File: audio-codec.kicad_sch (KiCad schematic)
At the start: 0 parts

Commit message: wip: not much to report yet
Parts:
- added U4: ~, symbol Library:TAC5112
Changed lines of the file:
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@@
 	(generator_version "8.0")
 	(paper "USLetter")
+	(symbol
+		(lib_id "Library:TAC5112")
+		(at 95.25 62.23 0)
+		(unit 1)
+		(exclude_from_sim no)
+		(in_bom yes)
+		(on_board yes)
+		(dnp no)
+		(fields_autoplaced yes)
+		(property "Reference" "U4"
+			(at 128.905 60.96 0)
+			(effects
+				(font
+					(size 1.27 1.27)
+				)
+			)
+		)
+		(property "Value" "~"
+			(at 128.905 63.5 0)
+			(effects
+				(font
+					(size 1.27 1.27)
+				)
+			)
+		)
+		(property "Footprint" ""
+			(at 95.25 62.23 0)
+			(effects
+				(font
+					(size 1.27 1.27)
+				)
+				(hide yes)
+			)
+		)
+		(property "Datasheet" ""
+			(at 95.25 62.23 0)
+			(effects
+				(font
+					(size 1.27 1.27)
+				)
+				(hide yes)
+			)
+		)
+		(property "Description" ""
+			(at 95.25 62.23 0)
+			(effects
+				(font
+					(size 1.27 1.27)
+				)
+				(hide yes)
+			)
+		)
+		(pin ""
+		)
+		(pin "23"
+		)
+		(pin "22"
+		)
+		(pin ""
+		)
+		(pin "12"
+		)
+		(pin "16"
+		)
+		(pin "14"
+		)
+		(pin "3"
+		)
+		(pin "5"
+		)
+		(pin "6"
+		)
+		(pin "15"
+		)
+		(pin "4"
+		)
+		(pin "19"
+		)
+		(pin "11"
+		)
+		(pin "20"
+		)
+		(pin "1"
+		)
+		(pin "18"
+		)
+		(pin "10"
+		)
+		(pin "24"
+		)
+		(pin "9"
+		)
+		(pin "8"
+		)
+		(pin "7"
+		)
+		(pin "13"
+		)
+		(pin "17"
+		)
+		(pin "21"
+		)
+		(pin "2"
+		)
+		(instances
+			(project ""
+				(path "/df100556-b288-4cb1-b69f-c0734132cb90/f904953f-335e-4512-b297-b8d4a411c7e1"
+					(reference "U4")
+					(unit 1)
+				)
+			)
+		)
+	)
 )

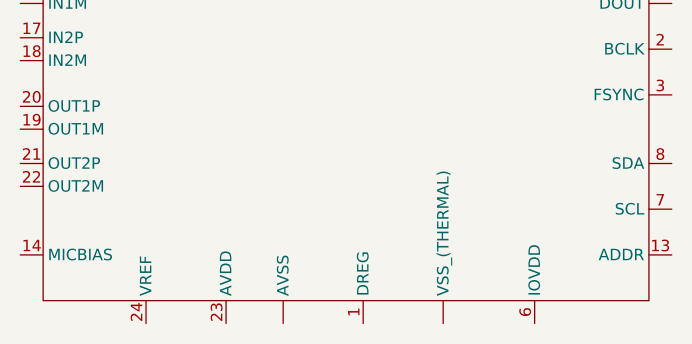
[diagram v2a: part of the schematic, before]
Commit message: almost done with clocking, need series terminators
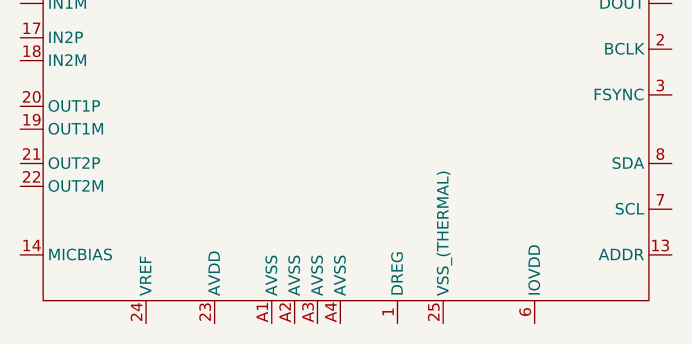
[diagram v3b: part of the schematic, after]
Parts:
- U4: footprint (none) -> Library:QFN-24_EP_4x4_Pitch0.5mm
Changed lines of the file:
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@@
 			)
 		)
-		(property "Footprint" ""
+		(property "Footprint" "Library:QFN-24_EP_4x4_Pitch0.5mm"
 			(at 95.25 62.23 0)
 			(effects
@@
 			)
 		)
-		(pin ""
+		(pin "A4"
 		)
 		(pin "23"
@@
 		(pin "22"
 		)
-		(pin ""
+		(pin "A2"
 		)
 		(pin "12"
@@
 		(pin "2"
 		)
+		(pin "A3"
+		)
+		(pin "A1"
+		)
+		(pin "25"
+		)
 		(instances

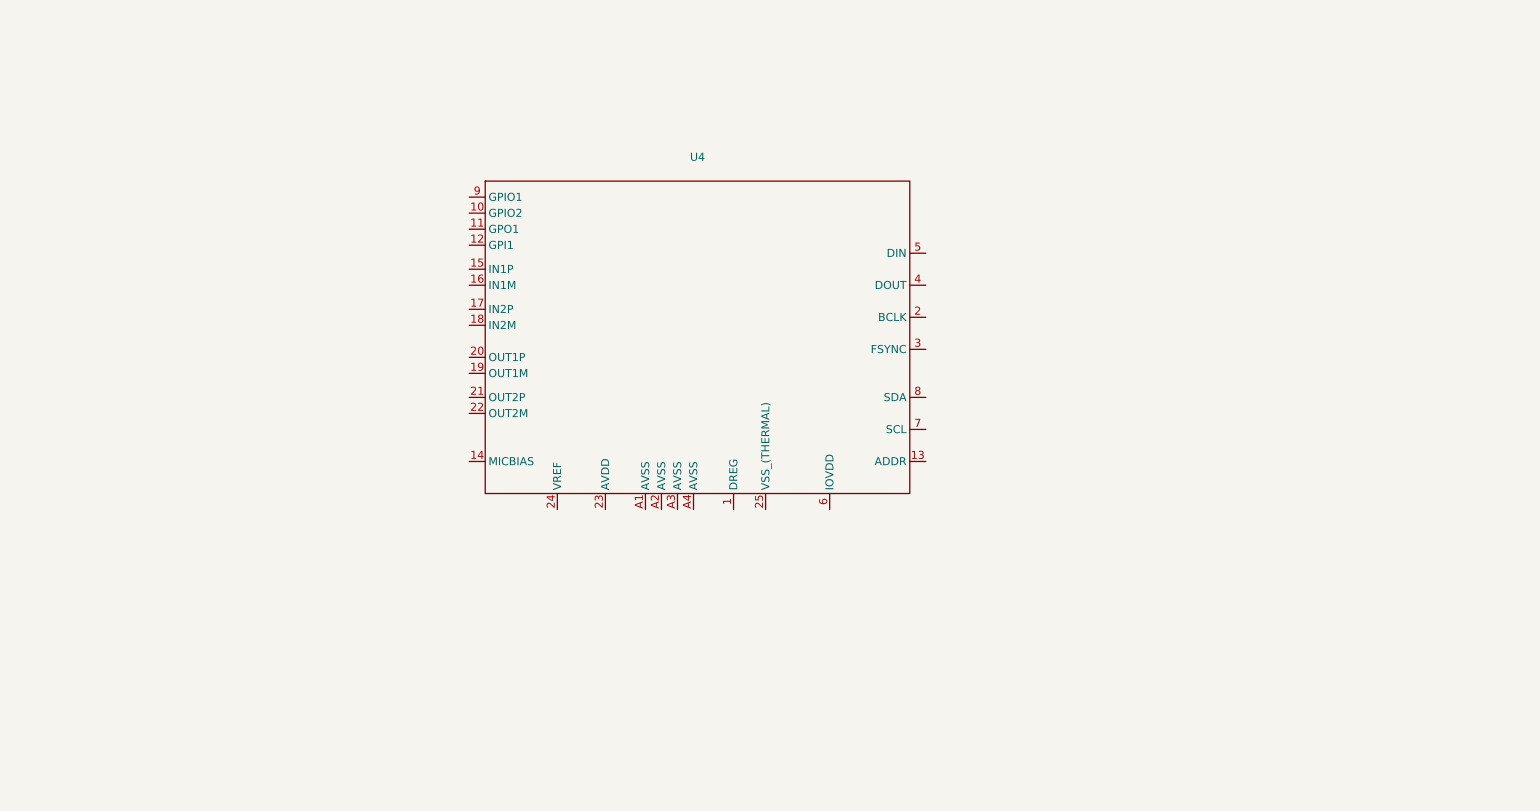
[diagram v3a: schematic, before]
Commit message: mostly done with schematic of mikrobus board
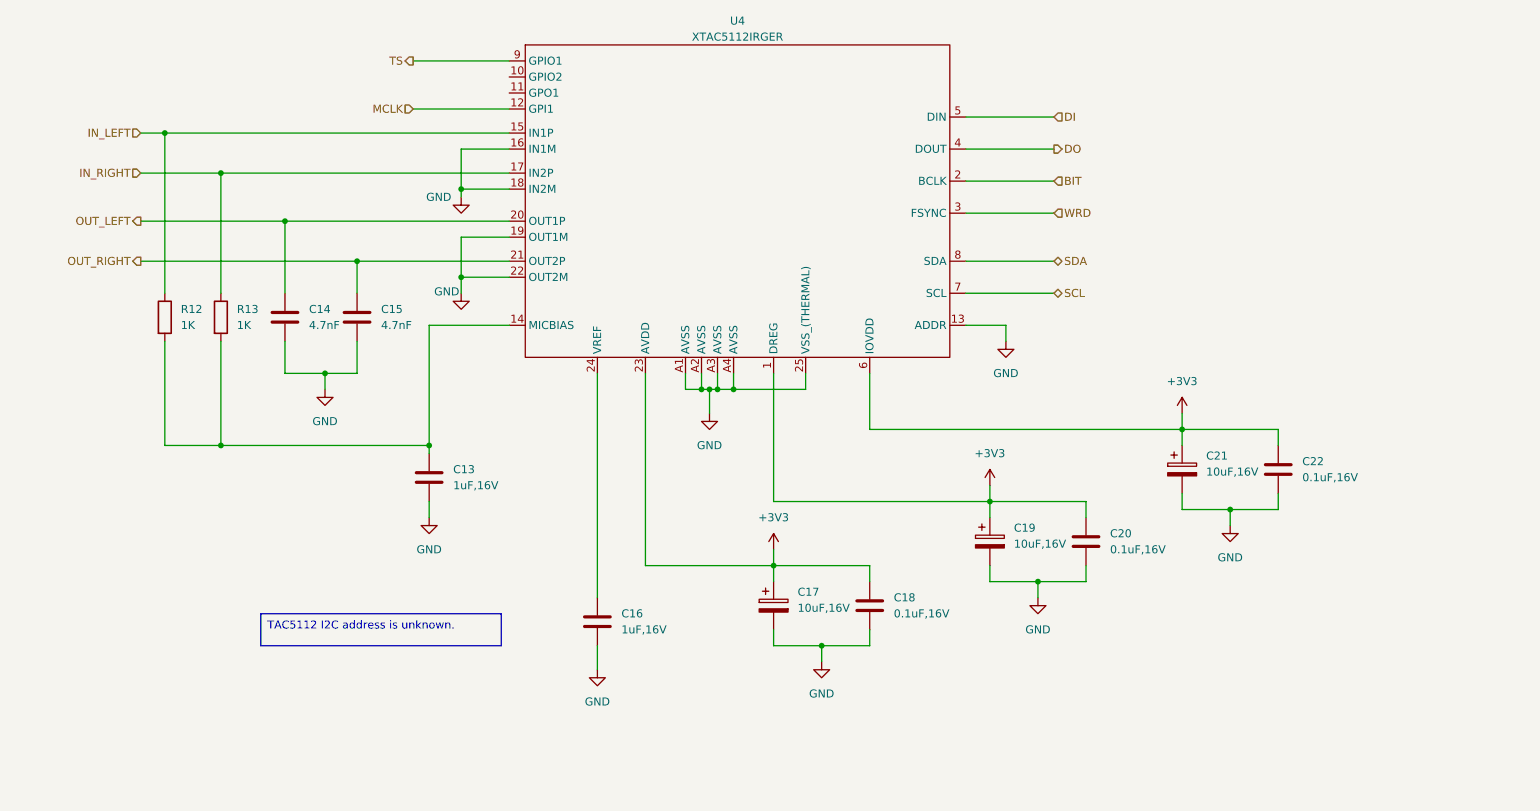
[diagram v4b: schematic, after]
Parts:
- added C13, C16: 1uF,16V, Capacitor_SMD:C_0603_1608Metric, symbol Device:C
- added C14, C15: 4.7nF, Capacitor_SMD:C_0603_1608Metric, symbol Device:C
- added C17, C19, C21: 10uF,16V, Capacitor_Tantalum_SMD:CP_EIA-1608-08_AVX-J, symbol Device:C_Polarized
- added C18, C20, C22: 0.1uF,16V, Capacitor_SMD:C_0603_1608Metric, symbol Device:C
- added R12, R13: 1K, Resistor_SMD:R_0603_1608Metric, symbol Device:R
- U4: value ~ -> XTAC5112IRGER
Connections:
- net +3V3: now reaches U4.1 (DREG)
- net +3V3: now also U4.23 (AVDD), U4.6 (IOVDD), C17.1, C18.1, C19.1, C20.1, C21.1, C22.1
- net MCLK: now reaches U4.12 (GPI1)
- net GND: now reaches U4.13 (ADDR)
- net GND: now also U4.16 (IN1M), U4.18 (IN2M), U4.19 (OUT1M), U4.22 (OUT2M), U4.25 (VSS_(THERMAL)), U4.A1 (AVSS), U4.A2 (AVSS), U4.A3 (AVSS), U4.A4 (AVSS), C13.2, C14.2, C15.2, C16.2, C17.2, C18.2, C19.2, C20.2, C21.2, C22.2
- net at U4.14 (MICBIAS): now also C13.1, R12.2, R13.2
- net IN_LEFT: now reaches U4.15 (IN1P)
- net IN_LEFT: now also R12.1
- net IN_RIGHT: now reaches U4.17 (IN2P)
- net IN_RIGHT: now also R13.1
- net BIT: now reaches U4.2 (BCLK)
- net OUT_LEFT: now reaches U4.20 (OUT1P)
- net OUT_LEFT: now also C14.1
- net OUT_RIGHT: now reaches U4.21 (OUT2P)
- net OUT_RIGHT: now also C15.1
- net at U4.24 (VREF): now also C16.1
- net WRD: now reaches U4.3 (FSYNC)
- net DO: now reaches U4.4 (DOUT)
- net DI: now reaches U4.5 (DIN)
- net SCL: now reaches U4.7 (SCL)
- net SDA: now reaches U4.8 (SDA)
- net TS: now reaches U4.9 (GPIO1)
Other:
- moved on the sheet: U4

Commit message: add 1-wire eeprom and a bit more
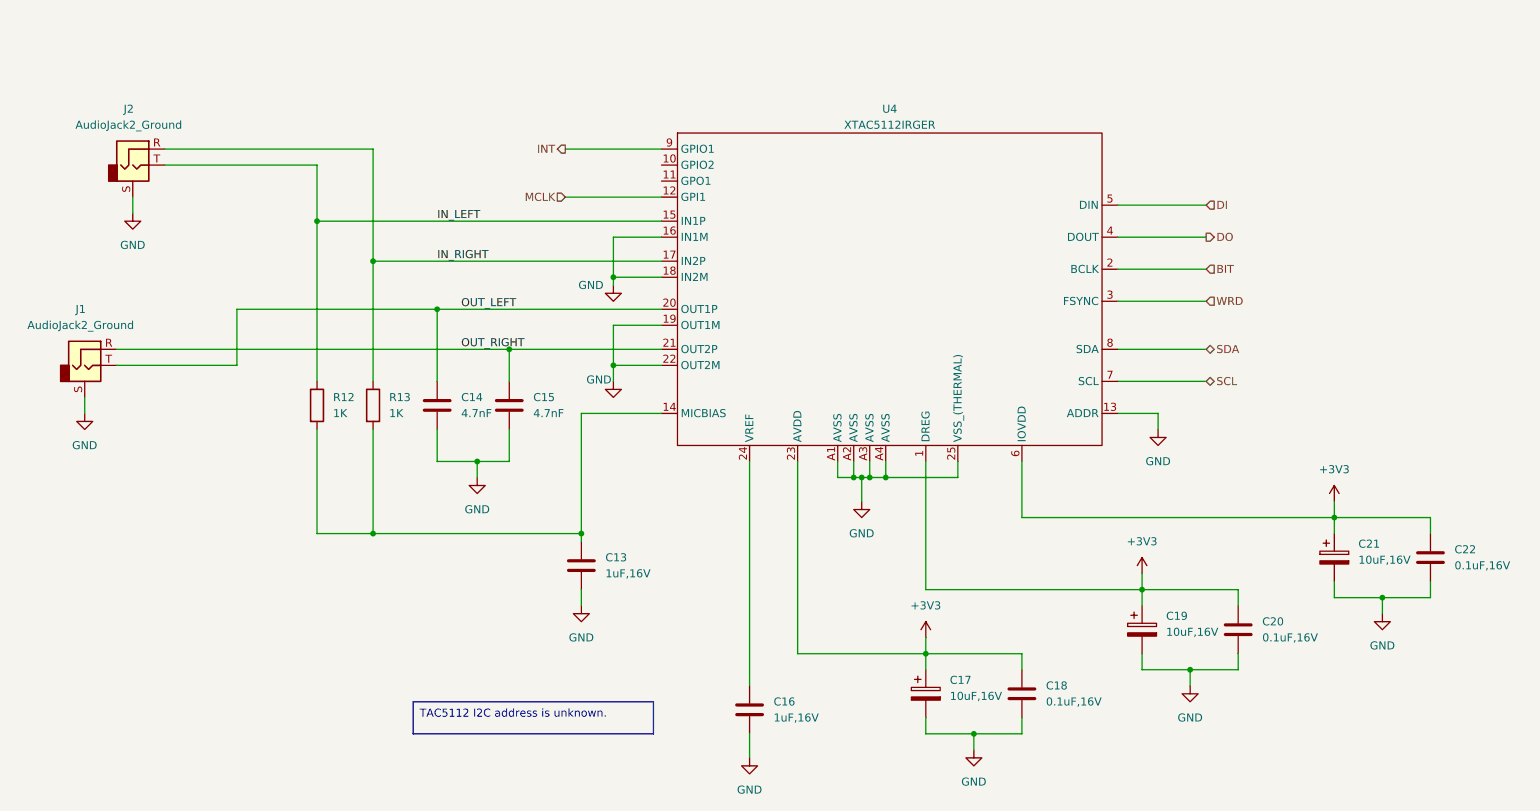
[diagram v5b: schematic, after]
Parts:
- added J1, J2: AudioJack2_Ground, Library:Jack_3.5mm_CUI_SJ-3523-SMT_Horizontal, symbol Connector_Audio:AudioJack2_Ground
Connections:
- net GND: now also J1.S, J2.S
- net IN_LEFT: now also J2.T
- net IN_RIGHT: now also J2.R
- net OUT_LEFT: now also J1.T
- net OUT_RIGHT: now also J1.R
- net TS renamed INT
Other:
- moved on the sheet: C13, C14, C15, C16, C17, C18, C19, C20, C21, C22, R12, R13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

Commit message: add extra labels to MB and title. specify project in CI file and update to Kicad 8.0.8
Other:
- company: (none) -> JKEmbedded, LLC
- title: (none) -> JKEmbedded Audio Board
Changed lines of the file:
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@@
 	(generator_version "8.0")
 	(paper "USLetter")
+	(title_block
+		(title "JKEmbedded Audio Board")
+		(company "JKEmbedded, LLC")
+	)
 	(junction
 		(at 172.72 152.4)

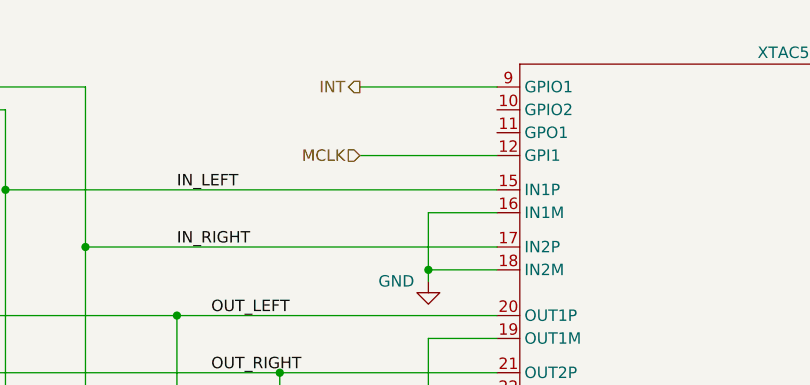
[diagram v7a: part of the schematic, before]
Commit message: worked through ERCs and updated PCB components
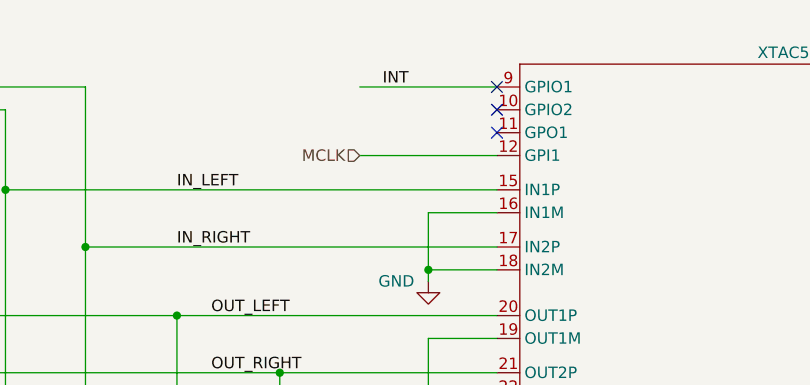
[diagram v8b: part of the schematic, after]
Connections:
- no-connect marks 0 -> 3
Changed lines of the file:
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@@
 		(color 0 0 0 0)
+	)
+	(no_connect
+		(at 123.19 64.77)
+	)
+	(no_connect
+		(at 123.19 62.23)
+	)
+	(no_connect
+		(at 123.19 59.69)
 	)
 	(wire
@@
 		)
 	)
+	(label "INT"
+		(at 110.49 59.69 0)
+		(effects
+			(font
+				(size 1.27 1.27)
+			)
+			(justify left bottom)
+		)
+	)
 	(label "OUT_RIGHT"
 		(at 91.44 91.44 0)
@@
 		)
 	)
-	(hierarchical_label "INT"
-		(shape output)
-		(at 107.95 59.69 180)
-		(effects
-			(font
-				(size 1.27 1.27)
-			)
-			(justify right)
-		)
-	)
